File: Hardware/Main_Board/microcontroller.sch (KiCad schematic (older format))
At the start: 53 parts

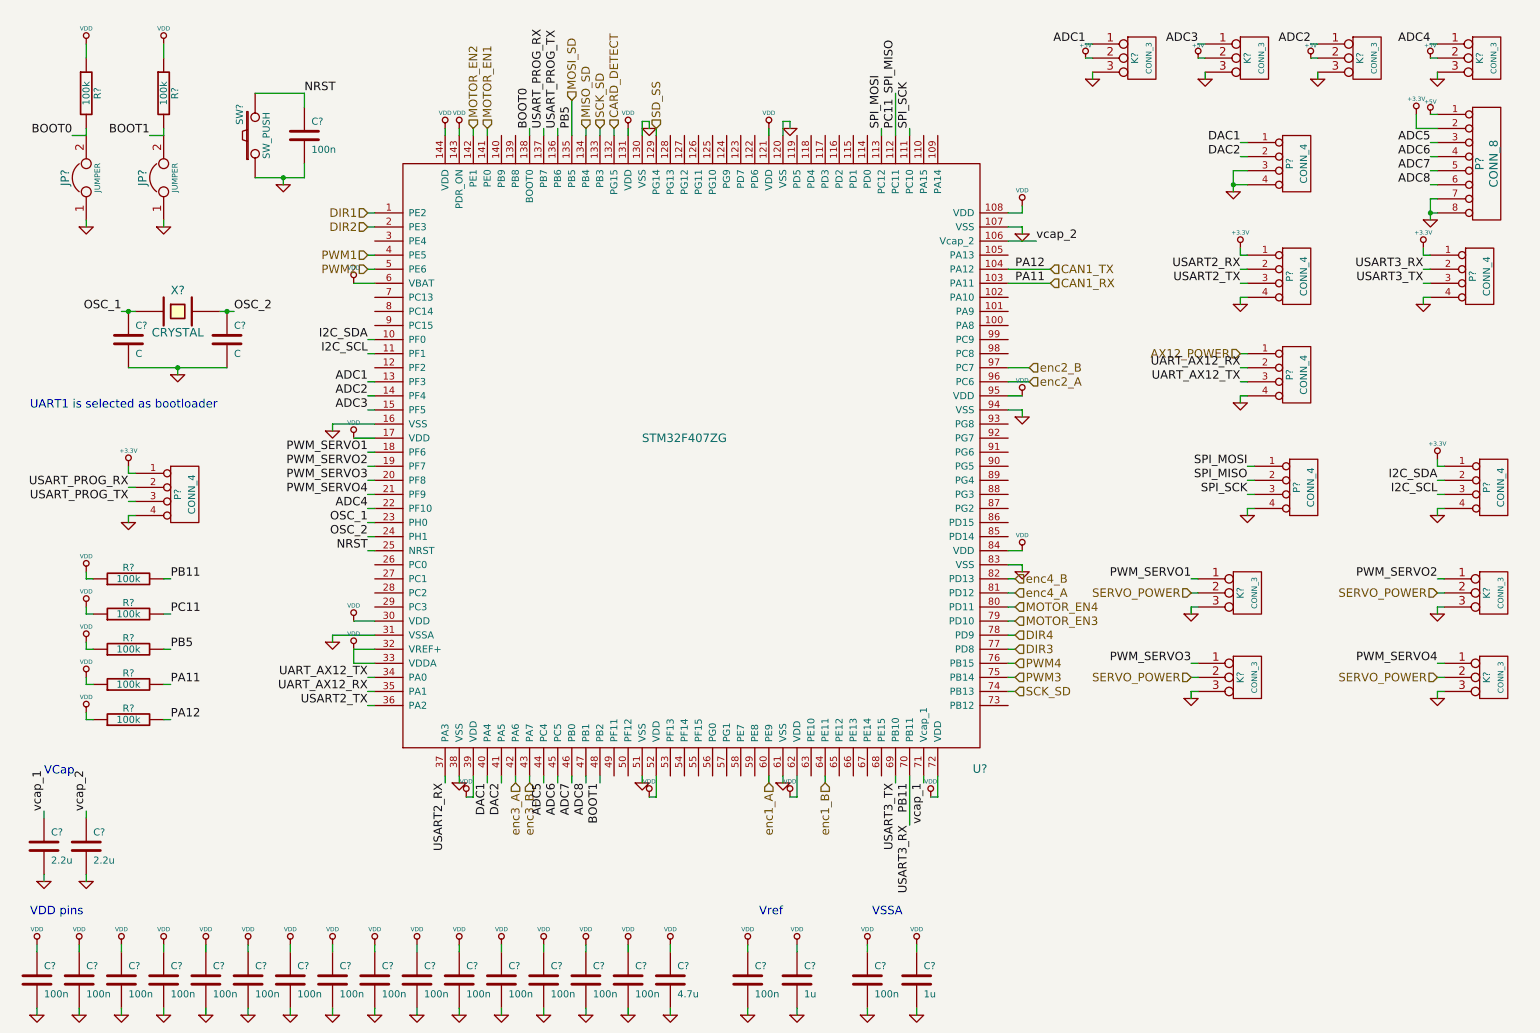
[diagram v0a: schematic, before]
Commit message: [HARDWARE] Add GPIO and led
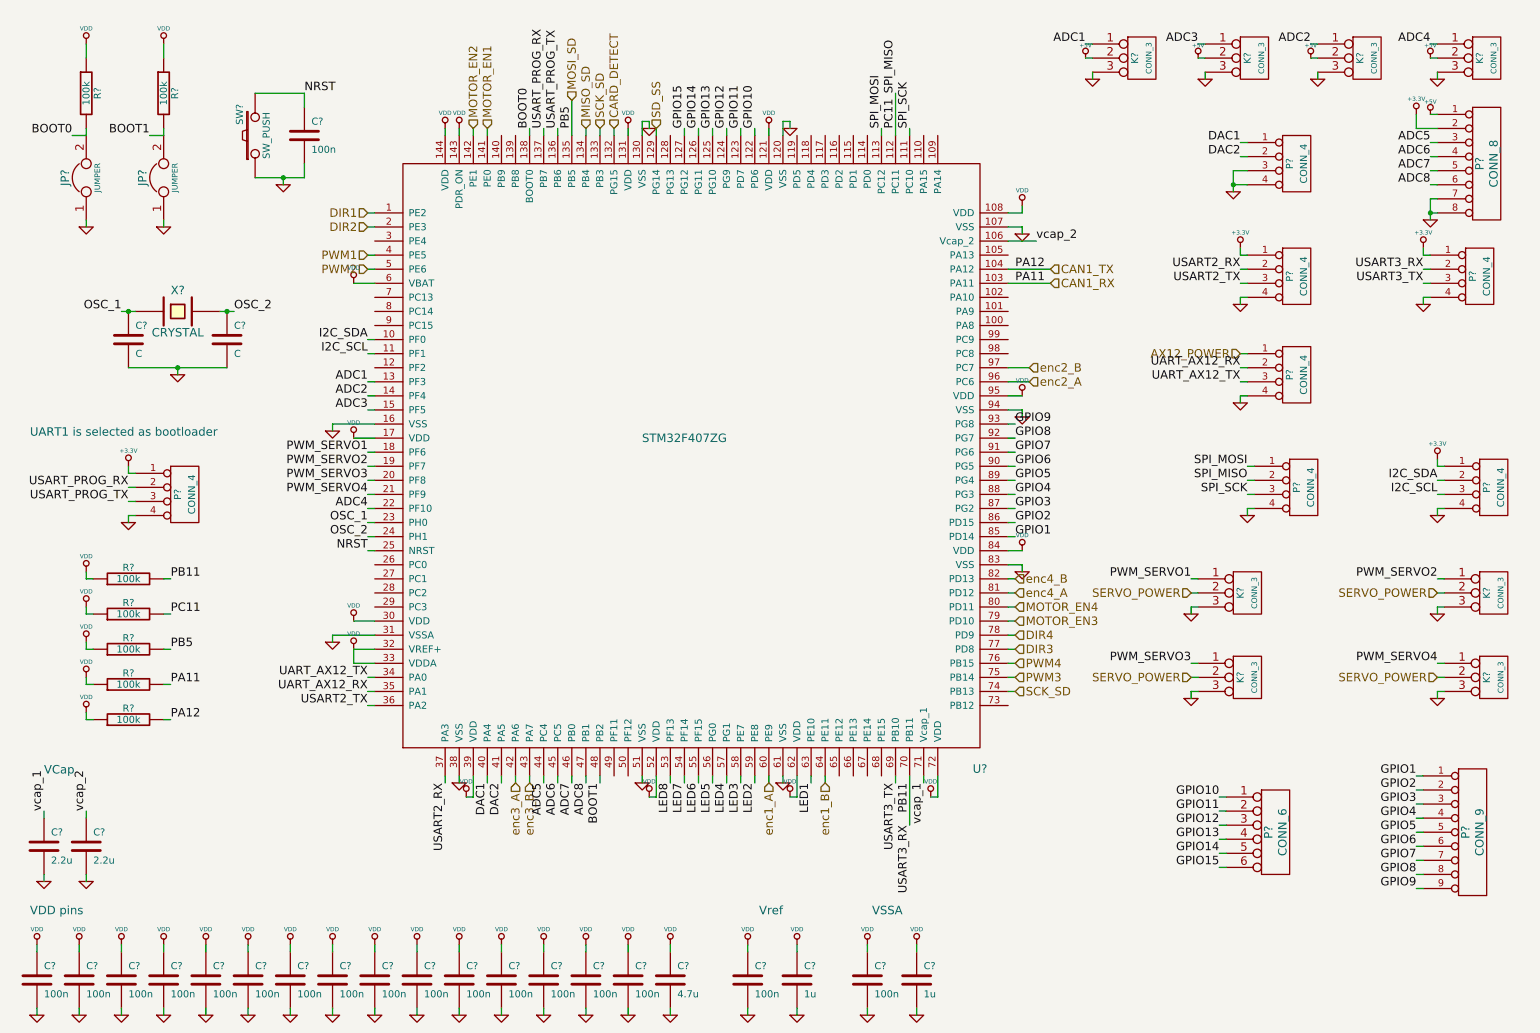
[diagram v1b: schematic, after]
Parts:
- added P?: CONN_9, symbol CONN_9
- added P?: CONN_6, symbol CONN_6
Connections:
- net GPIO10: now reaches U?.122 (PD6)
- net GPIO10: now also P?.1
- net GPIO11: now reaches U?.123 (PD7)
- net GPIO11: now also P?.2
- net GPIO12: now reaches U?.124 (PG9)
- net GPIO12: now also P?.3
- net GPIO13: now reaches U?.125 (PG10)
- net GPIO13: now also P?.4
- net GPIO14: now reaches U?.126 (PG11)
- net GPIO14: now also P?.5
- net GPIO15: now reaches U?.127 (PG12)
- net GPIO15: now also P?.6
- net LED8: now reaches U?.53 (PF13)
- net LED7: now reaches U?.54 (PF14)
- net LED6: now reaches U?.55 (PF15)
- net LED5: now reaches U?.56 (PG0)
- net LED4: now reaches U?.57 (PG1)
- net LED3: now reaches U?.58 (PE7)
- net LED2: now reaches U?.59 (PE8)
- net LED1: now reaches U?.63 (PE10)
- net GPIO1: now reaches U?.85 (PD14)
- net GPIO1: now also P?.1 (P1)
- net GPIO2: now reaches U?.86 (PD15)
- net GPIO2: now also P?.2 (P2)
- net GPIO3: now reaches U?.87 (PG2)
- net GPIO3: now also P?.3 (P3)
- net GPIO4: now reaches U?.88 (PG3)
- net GPIO4: now also P?.4 (P4)
- net GPIO5: now reaches U?.89 (PG4)
- net GPIO5: now also P?.5 (P5)
- net GPIO6: now reaches U?.90 (PG5)
- net GPIO6: now also P?.6 (P6)
- net GPIO7: now reaches U?.91 (PG6)
- net GPIO7: now also P?.7 (P7)
- net GPIO8: now reaches U?.92 (PG7)
- net GPIO8: now also P?.8 (P8)
- net GPIO9: now reaches U?.93 (PG8)
- net GPIO9: now also P?.9 (P9)
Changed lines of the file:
@@
-EESchema Schematic File Version 2  date mar. 08 oct. 2013 19:56:47 CEST
+EESchema Schematic File Version 2  date mer. 09 oct. 2013 08:38:21 CEST
 LIBS:power
 LIBS:device
@@
 Sheet 2 5
 Title ""
-Date "8 oct 2013"
+Date "9 oct 2013"
 Rev ""
 Comp ""
@@
 $EndDescr
 Wire Wire Line
+	9050 6650 9000 6650
+Wire Wire Line
+	9050 6450 9000 6450
+Wire Wire Line
+	9050 6250 9000 6250
+Wire Wire Line
+	10400 6800 10450 6800
+Wire Wire Line
+	10400 6600 10450 6600
+Wire Wire Line
+	10400 6400 10450 6400
+Wire Wire Line
+	10400 6200 10450 6200
+Wire Wire Line
+	10400 6000 10450 6000
+Wire Wire Line
+	5300 1400 5300 1450
+Wire Wire Line
+	5600 1400 5600 1450
+Wire Wire Line
+	5500 1450 5500 1400
+Wire Wire Line
+	5200 6050 5200 6000
+Wire Wire Line
+	5400 6000 5400 6050
+Wire Wire Line
+	5600 6050 5600 6000
+Wire Wire Line
+	6100 6050 6100 6000
+Wire Wire Line
+	7550 4200 7500 4200
+Wire Wire Line
+	7500 4000 7550 4000
+Wire Wire Line
+	7500 3800 7550 3800
+Wire Wire Line
+	7500 3600 7550 3600
+Wire Wire Line
 	5000 1450 5000 1400
 Wire Wire Line
@@
 Wire Wire Line
 	4700 1450 4700 1400
+Wire Wire Line
+	7550 3500 7500 3500
+Wire Wire Line
+	7550 3700 7500 3700
+Wire Wire Line
+	7550 3900 7500 3900
+Wire Wire Line
+	7500 4100 7550 4100
+Wire Wire Line
+	7500 4300 7550 4300
+Wire Wire Line
+	5700 6050 5700 6000
+Wire Wire Line
+	5500 6050 5500 6000
+Wire Wire Line
+	5300 6000 5300 6050
+Wire Wire Line
+	5100 6000 5100 6050
+Wire Wire Line
+	5700 1400 5700 1450
+Wire Wire Line
+	5400 1400 5400 1450
+Wire Wire Line
+	5200 1400 5200 1450
+Wire Wire Line
+	10450 6100 10400 6100
+Wire Wire Line
+	10450 6300 10400 6300
+Wire Wire Line
+	10450 6500 10400 6500
+Wire Wire Line
+	10450 6700 10400 6700
+Wire Wire Line
+	9000 6150 9050 6150
+Wire Wire Line
+	9000 6350 9050 6350
+Wire Wire Line
+	9000 6550 9050 6550
+Text Label 9000 6150 2    60   ~ 0
+GPIO10
+Text Label 9000 6250 2    60   ~ 0
+GPIO11
+Text Label 9000 6350 2    60   ~ 0
+GPIO12
+Text Label 9000 6450 2    60   ~ 0
+GPIO13
+Text Label 9000 6550 2    60   ~ 0
+GPIO14
+Text Label 9000 6650 2    60   ~ 0
+GPIO15
+$Comp
+L CONN_6 P?
+U 1 1 5254F91A
+P 9400 6400
+F 0 "P?" V 9350 6400 60  0000 C CNN
+F 1 "CONN_6" V 9450 6400 60  0000 C CNN
+	1    9400 6400
+	1    0    0    -1
+$EndComp
+Text Label 10400 6800 2    60   ~ 0
+GPIO9
+Text Label 10400 6700 2    60   ~ 0
+GPIO8
+Text Label 10400 6600 2    60   ~ 0
+GPIO7
+Text Label 10400 6500 2    60   ~ 0
+GPIO6
+Text Label 10400 6400 2    60   ~ 0
+GPIO5
+Text Label 10400 6300 2    60   ~ 0
+GPIO4
+Text Label 10400 6200 2    60   ~ 0
+GPIO3
+Text Label 10400 6100 2    60   ~ 0
+GPIO2
+Text Label 10400 6000 2    60   ~ 0
+GPIO1
+$Comp
+L CONN_9 P?
+U 1 1 5254F8D3
+P 10800 6400
+F 0 "P?" V 10750 6400 60  0000 C CNN
+F 1 "CONN_9" V 10850 6400 60  0000 C CNN
+	1    10800 6400
+	1    0    0    -1
+$EndComp
+Text Label 5200 1400 1    60   ~ 0
+GPIO15
+Text Label 5300 1400 1    60   ~ 0
+GPIO14
+Text Label 5400 1400 1    60   ~ 0
+GPIO13
+Text Label 5500 1400 1    60   ~ 0
+GPIO12
+Text Label 5600 1400 1    60   ~ 0
+GPIO11
+Text Label 5700 1400 1    60   ~ 0
+GPIO10
+Text Label 5100 6050 3    60   ~ 0
+LED8
+Text Label 5200 6050 3    60   ~ 0
+LED7
+Text Label 5300 6050 3    60   ~ 0
+LED6
+Text Label 5400 6050 3    60   ~ 0
+LED5
+Text Label 5500 6050 3    60   ~ 0
+LED4
+Text Label 5600 6050 3    60   ~ 0
+LED3
+Text Label 5700 6050 3    60   ~ 0
+LED2
+Text Label 6100 6050 3    60   ~ 0
+LED1
+Text Label 7550 3500 0    60   ~ 0
+GPIO9
+Text Label 7550 3600 0    60   ~ 0
+GPIO8
+Text Label 7550 3700 0    60   ~ 0
+GPIO7
+Text Label 7550 3800 0    60   ~ 0
+GPIO6
+Text Label 7550 3900 0    60   ~ 0
+GPIO5
+Text Label 7550 4000 0    60   ~ 0
+GPIO4
+Text Label 7550 4100 0    60   ~ 0
+GPIO3
+Text Label 7550 4200 0    60   ~ 0
+GPIO2
+Text Label 7550 4300 0    60   ~ 0
+GPIO1
 Text HLabel 5000 1400 1    60   Input ~ 0
 SD_SS
@@
 	1    0    0    -1
 $EndComp
-Text Notes 550  3400 0    60   ~ 0
+Text Notes 550  3600 0    60   ~ 0
 UART1 is selected as bootloader
 Text Label 7550 2500 0    60   ~ 0

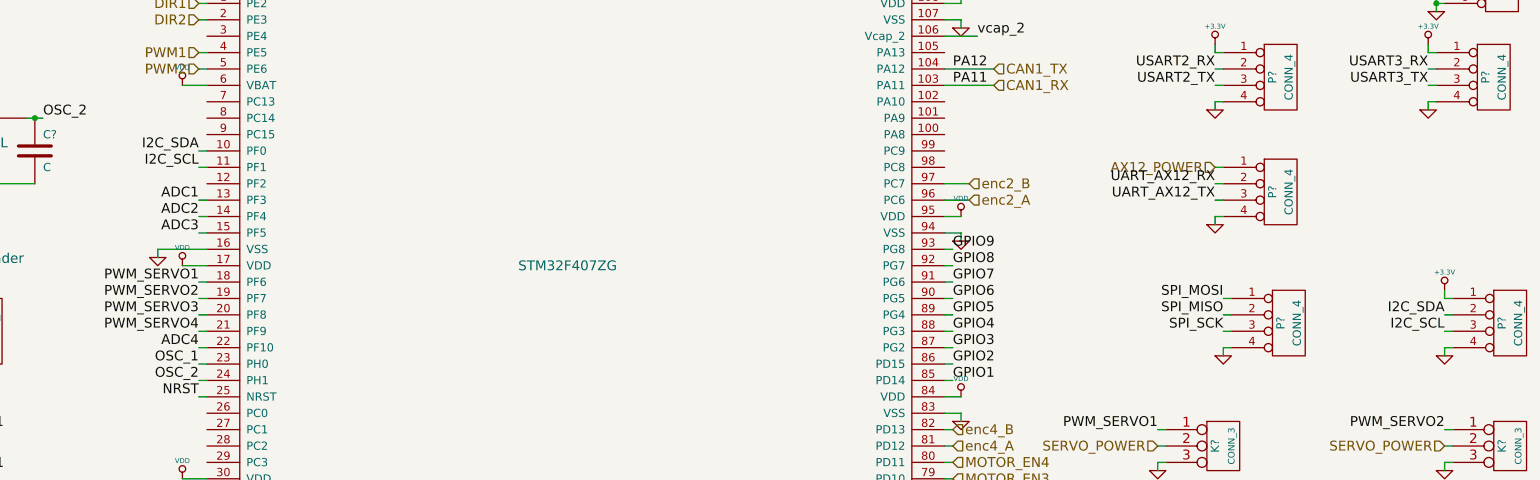
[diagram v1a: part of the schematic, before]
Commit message: [HARDWARE] Add 1 I2C interface
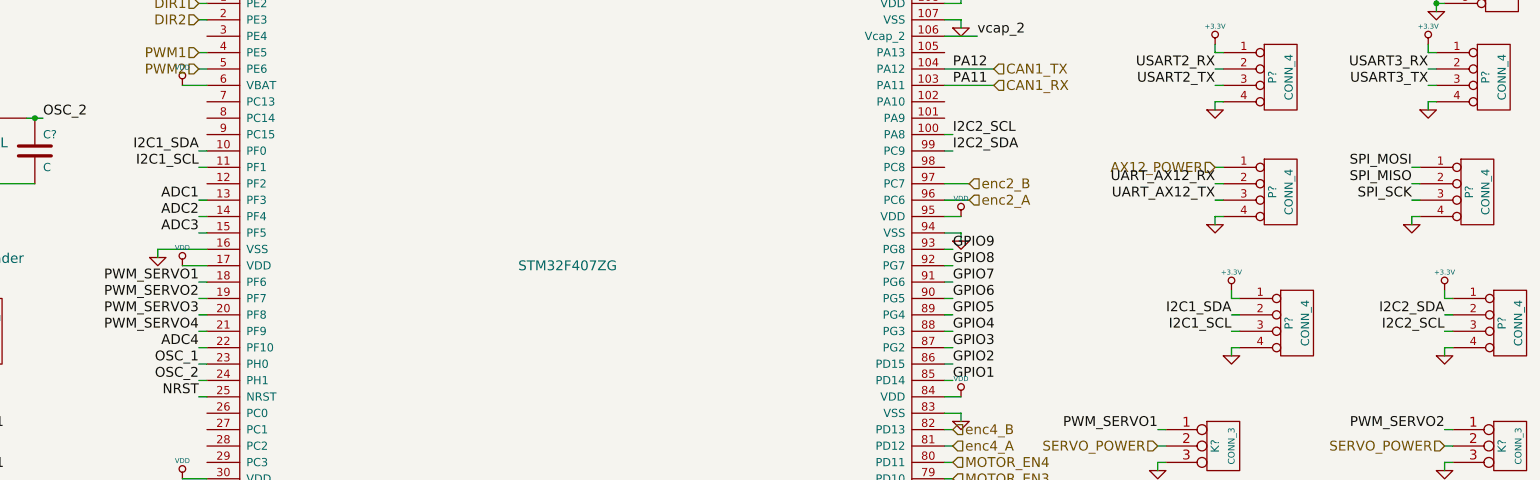
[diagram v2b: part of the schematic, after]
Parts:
- added P?: CONN_4, symbol CONN_4
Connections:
- net +3.3V: now also P?.1 (P1)
- net GND: now also P?.4 (P4)
- net I2C2_SCL: now reaches U?.100 (PA8)
- net I2C2_SCL: now also P?.3 (P3)
- net I2C2_SDA: now reaches U?.99 (PC9)
- net I2C2_SDA: now also P?.2 (P2)
- net I2C_SCL renamed I2C1_SCL
- net I2C1_SCL: now also P?.3 (P3); no longer P?.3 (P3)
- net I2C_SDA renamed I2C1_SDA
- net I2C1_SDA: now also P?.2 (P2); no longer P?.2 (P2)
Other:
- moved on the sheet: P?
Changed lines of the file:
@@
-EESchema Schematic File Version 2  date mer. 09 oct. 2013 08:38:21 CEST
+EESchema Schematic File Version 2  date mer. 09 oct. 2013 08:43:14 CEST
 LIBS:power
 LIBS:device
@@
 Comment4 ""
 $EndDescr
+$Comp
+L CONN_4 P?
+U 1 1 5254FAAB
+P 9650 3950
+F 0 "P?" V 9600 3950 50  0000 C CNN
+F 1 "CONN_4" V 9700 3950 50  0000 C CNN
+	1    9650 3950
+	1    0    0    -1
+$EndComp
+$Comp
+L GND #PWR?
+U 1 1 5254FAAA
+P 9250 4150
+F 0 "#PWR?" H 9250 4150 30  0001 C CNN
+F 1 "GND" H 9250 4080 30  0001 C CNN
+	1    9250 4150
+	1    0    0    -1
+$EndComp
+$Comp
+L +3.3V #PWR?
+U 1 1 5254FAA9
+P 9250 3750
+F 0 "#PWR?" H 9250 3710 30  0001 C CNN
+F 1 "+3.3V" H 9250 3860 30  0000 C CNN
+	1    9250 3750
+	1    0    0    -1
+$EndComp
+Text Label 9250 3900 2    60   ~ 0
+I2C1_SDA
+Text Label 9250 4000 2    60   ~ 0
+I2C1_SCL
+Wire Wire Line
+	9300 4000 9250 4000
+Wire Wire Line
+	9250 4100 9300 4100
+Wire Wire Line
+	9250 4150 9250 4100
+Wire Wire Line
+	9250 3800 9250 3750
+Wire Wire Line
+	9300 3800 9250 3800
+Wire Wire Line
+	9250 3900 9300 3900
+Wire Wire Line
+	7550 2800 7500 2800
 Wire Wire Line
 	9050 6650 9000 6650
@@
 	3000 3000 2950 3000
 Wire Wire Line
-	9200 4000 9250 4000
-Wire Wire Line
-	9200 3800 9250 3800
+	10350 3200 10400 3200
+Wire Wire Line
+	10350 3000 10400 3000
 Wire Wire Line
 	6600 1400 6600 1450
@@
 	6800 1400 6800 1450
 Wire Wire Line
-	9200 4150 9200 4100
-Wire Wire Line
-	9200 4100 9250 4100
-Wire Wire Line
-	9250 3900 9200 3900
+	10350 3350 10350 3300
+Wire Wire Line
+	10350 3300 10400 3300
+Wire Wire Line
+	10400 3100 10350 3100
 Wire Wire Line
 	2950 2900 3000 2900
@@
 Wire Wire Line
 	9000 6550 9050 6550
+Wire Wire Line
+	7550 2900 7500 2900
+Text Label 7550 2800 0    60   ~ 0
+I2C2_SCL
+Text Label 7550 2900 0    60   ~ 0
+I2C2_SDA
 Text Label 9000 6150 2    60   ~ 0
 GPIO10
@@
 PWM_SERVO1
 Text Label 10550 4000 2    60   ~ 0
-I2C_SCL
+I2C2_SCL
 Text Label 10550 3900 2    60   ~ 0
-I2C_SDA
+I2C2_SDA
 $Comp
 L +3.3V #PWR?
@@
 $EndComp
 Text Label 2950 3000 2    60   ~ 0
-I2C_SCL
+I2C1_SCL
 Text Label 2950 2900 2    60   ~ 0
-I2C_SDA
-Text Label 9200 3900 2    60   ~ 0
+I2C1_SDA
+Text Label 10350 3100 2    60   ~ 0
 SPI_MISO
-Text Label 9200 3800 2    60   ~ 0
+Text Label 10350 3000 2    60   ~ 0
 SPI_MOSI
-Text Label 9200 4000 2    60   ~ 0
+Text Label 10350 3200 2    60   ~ 0
 SPI_SCK
 $Comp
 L GND #PWR?
 U 1 1 52519BF1
-P 9200 4150
-F 0 "#PWR?" H 9200 4150 30  0001 C CNN
-F 1 "GND" H 9200 4080 30  0001 C CNN
-	1    9200 4150
+P 10350 3350
+F 0 "#PWR?" H 10350 3350 30  0001 C CNN
+F 1 "GND" H 10350 3280 30  0001 C CNN
+	1    10350 3350
 	1    0    0    -1
 $EndComp
@@
 L CONN_4 P?
 U 1 1 52519BEA
-P 9600 3950
-F 0 "P?" V 9550 3950 50  0000 C CNN
-F 1 "CONN_4" V 9650 3950 50  0000 C CNN
-	1    9600 3950
-	1    0    0    -1
-$EndComp
+P 10750 3150
+F 0 "P?" V 10700 3150 50  0000 C CNN
+F 1 "CONN_4" V 10800 3150 50  0000 C CNN
+	1    10750 3150
+	1    0    0    -1
+$EndComp
